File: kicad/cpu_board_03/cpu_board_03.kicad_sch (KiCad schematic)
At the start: 60 parts, among them J1 DIN41612_02x32_AC, J10 PLD_aux, J11 Conn_01x09, J6 Conn_01x02_Socket, J9 Ram1 Enable, SW1 SW_Reset, SW2 SW_PWR, U1 W65C02SxP, U10 74HC245, U11 74HC245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

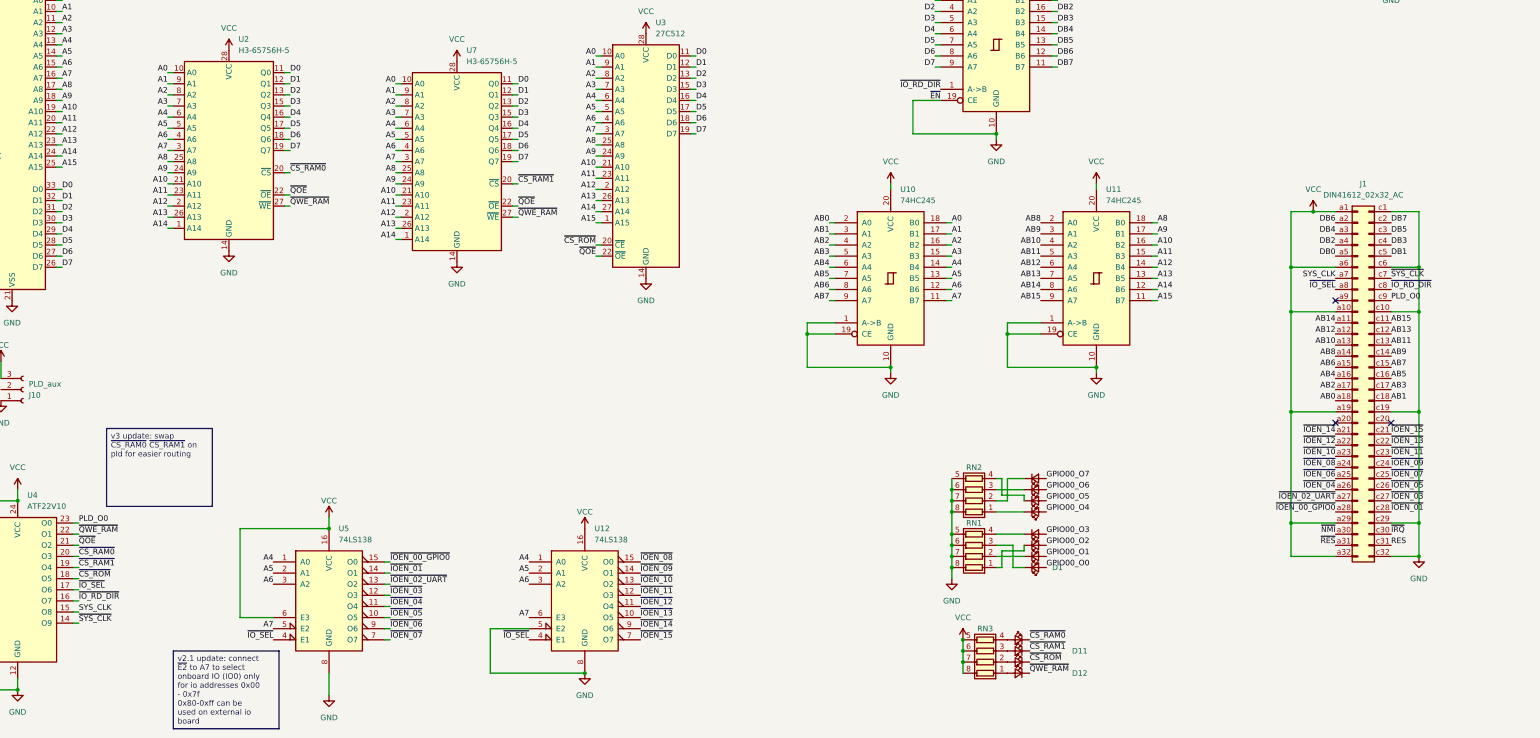
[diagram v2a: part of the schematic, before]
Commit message: update label names
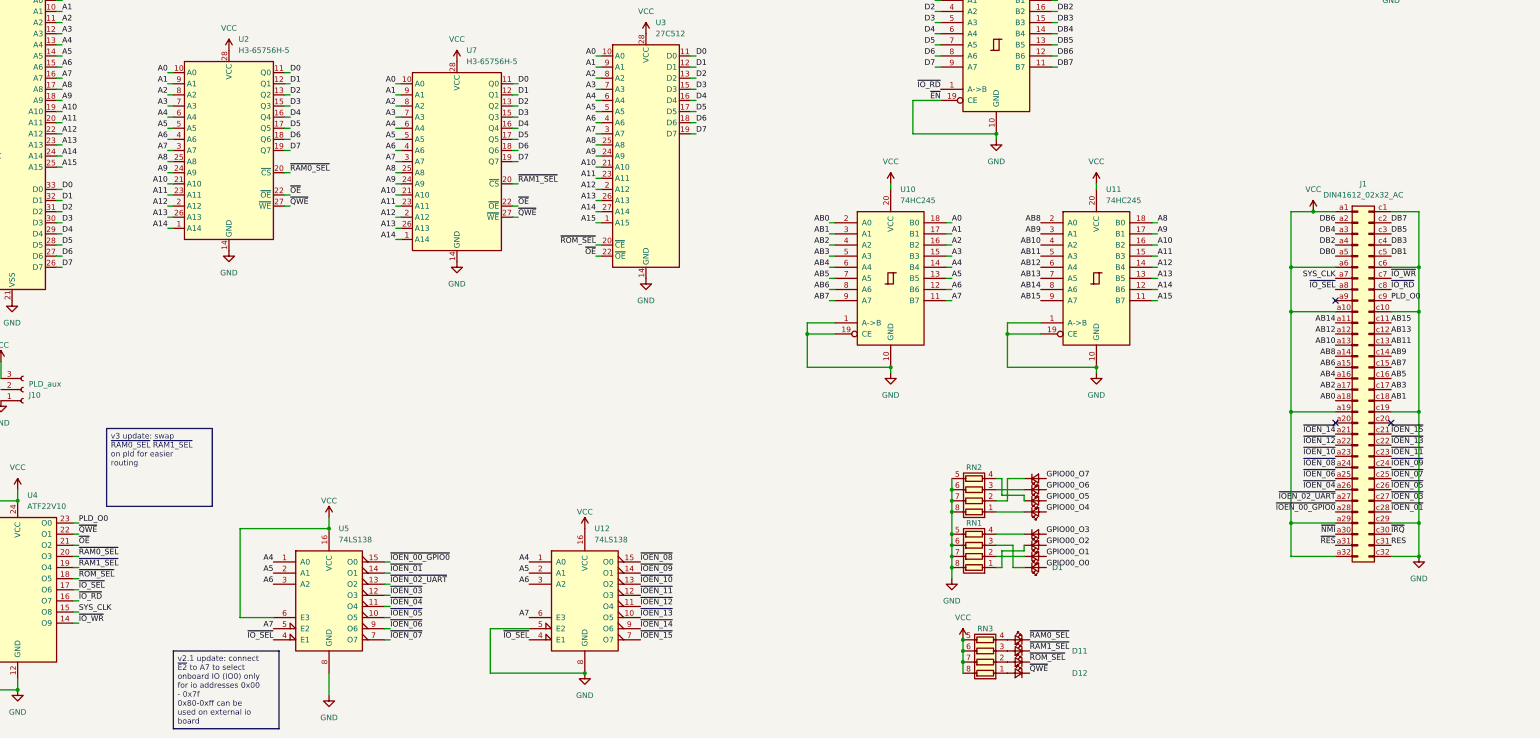
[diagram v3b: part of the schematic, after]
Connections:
- net ~{CS_RAM0} renamed ~{RAM0_SEL}
- net ~{CS_RAM1} renamed ~{RAM1_SEL}
- net ~{CS_ROM} renamed ~{ROM_SEL}
- net ~{IO_RD_DIR} renamed ~{IO_RD}
- net ~{QOE} renamed ~{OE}
- net ~{QWE_RAM} renamed ~{QWE}
- net ~{SYS_CLK} renamed ~{IO_WR}
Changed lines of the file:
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@@
 		)
 	)
-	(text_box "v3 update: swap ~{CS_RAM0} ~{CS_RAM1} on pld for easier routing"
+	(text_box "v3 update: swap ~{RAM0_SEL} ~{RAM1_SEL} on pld for easier routing"
 		(exclude_from_sim no)
 		(at 68.58 214.63 0)
@@
 		)
 	)
-	(label "~{IO_RD_DIR}"
+	(label "~{IO_RD}"
 		(at 361.95 182.88 0)
 		(effects
@@
 		)
 	)
-	(label "~{QOE}"
+	(label "~{OE}"
 		(at 162.56 163.83 0)
 		(effects
@@
 		)
 	)
-	(label "~{IO_RD_DIR}"
+	(label "~{IO_RD}"
 		(at 259.08 137.16 180)
 		(effects
@@
 		)
 	)
-	(label "~{QOE}"
+	(label "~{OE}"
 		(at 62.23 241.3 0)
 		(effects
@@
 		)
 	)
-	(label "~{CS_RAM1}"
+	(label "~{RAM1_SEL}"
 		(at 62.23 246.38 0)
 		(effects
@@
 		)
 	)
-	(label "~{CS_RAM0}"
+	(label "~{RAM0_SEL}"
 		(at 279.4 262.89 0)
 		(effects
@@
 		)
 	)
-	(label "~{QWE_RAM}"
+	(label "~{QWE}"
 		(at 110.49 163.83 0)
 		(effects
@@
 		)
 	)
-	(label "~{QWE_RAM}"
+	(label "~{QWE}"
 		(at 62.23 238.76 0)
 		(effects
@@
 		)
 	)
-	(label "~{CS_RAM0}"
+	(label "~{RAM0_SEL}"
 		(at 62.23 243.84 0)
 		(effects
@@
 		)
 	)
-	(label "~{CS_RAM0}"
+	(label "~{RAM0_SEL}"
 		(at 110.49 156.21 0)
 		(effects
@@
 		)
 	)
-	(label "~{CS_RAM1}"
+	(label "~{RAM1_SEL}"
 		(at 279.4 265.43 0)
 		(effects
@@
 		)
 	)
-	(label "~{QOE}"
+	(label "~{OE}"
 		(at 110.49 161.29 0)
 		(effects
@@
 		)
 	)
-	(label "~{QWE_RAM}"
+	(label "~{QWE}"
 		(at 279.4 270.51 0)
 		(effects
@@
 		)
 	)
-	(label "~{SYS_CLK}"
+	(label "~{IO_WR}"
 		(at 62.23 259.08 0)
 		(effects
@@
 		)
 	)
-	(label "~{IO_RD_DIR}"
+	(label "~{IO_RD}"
 		(at 62.23 254 0)
 		(effects
@@
 		)
 	)
-	(label "~{QWE_RAM}"
+	(label "~{QWE}"
 		(at 162.56 166.37 0)
 		(effects
@@
 		)
 	)
-	(label "~{CS_ROM}"
+	(label "~{ROM_SEL}"
 		(at 62.23 248.92 0)
 		(effects
@@
 		)
 	)
-	(label "~{QOE}"
+	(label "~{OE}"
 		(at 180.34 175.26 180)
 		(effects
@@
 		)
 	)
-	(label "~{CS_ROM}"
+	(label "~{ROM_SEL}"
 		(at 180.34 172.72 180)
 		(effects
@@
 		)
 	)
-	(label "~{SYS_CLK}"
+	(label "~{IO_WR}"
 		(at 361.95 180.34 0)
 		(effects
@@
 		)
 	)
-	(label "~{CS_ROM}"
+	(label "~{ROM_SEL}"
 		(at 279.4 267.97 0)
 		(effects
@@
 		)
 	)
-	(label "~{CS_RAM1}"
+	(label "~{RAM1_SEL}"
 		(at 162.56 158.75 0)
 		(effects

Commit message: update pcb
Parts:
- removed U14: 74AHC1G04, Package_TO_SOT_SMD:SOT-23-5_HandSoldering, symbol 74xGxx:74AHC1G04
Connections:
- net ~{IO_WR}: now also U13.1
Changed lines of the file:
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@@
 	)
 	(no_connect
+		(at 349.25 185.42)
+	)
+	(no_connect
 		(at 349.25 213.36)
 	)
@@
 	)
 	(no_connect
-		(at 349.25 185.42)
-	)
-	(no_connect
 		(at 54.61 52.07)
 	)
@@
 		)
 	)
+	(label "~{IO_WR}"
+		(at 313.69 80.01 180)
+		(effects
+			(font
+				(size 1.27 1.27)
+			)
+			(justify right bottom)
+		)
+	)
 	(label "GPIO00_O4"
 		(at 283.21 233.68 0)
@@
 		)
 	)
-	(label "CLOCK"
-		(at 285.75 80.01 180)
-		(effects
-			(font
-				(size 1.27 1.27)
-			)
-			(justify right bottom)
-		)
-	)
 	(label "A10"
 		(at 308.61 172.72 0)
@@
 	)
 	(symbol
-		(lib_id "74xGxx:74AHC1G04")
-		(at 300.99 80.01 0)
-		(unit 1)
-		(exclude_from_sim no)
-		(in_bom yes)
-		(on_board yes)
-		(dnp no)
-		(fields_autoplaced yes)
-		(property "Reference" "U14"
-			(at 313.69 73.5898 0)
-			(effects
-				(font
-					(size 1.27 1.27)
-				)
-			)
-		)
-		(property "Value" "74AHC1G04"
-			(at 313.69 76.1298 0)
-			(effects
-				(font
-					(size 1.27 1.27)
-				)
-			)
-		)
-		(property "Footprint" "Package_TO_SOT_SMD:SOT-23-5_HandSoldering"
-			(at 300.99 80.01 0)
-			(effects
-				(font
-					(size 1.27 1.27)
-				)
-				(hide yes)
-			)
-		)
-		(property "Datasheet" "http://www.ti.com/lit/sg/scyt129e/scyt129e.pdf"
-			(at 300.99 80.01 0)
-			(effects
-				(font
-					(size 1.27 1.27)
-				)
-				(hide yes)
-			)
-		)
-		(property "Description" "Single NOT Gate, Low-Voltage CMOS"
-			(at 300.99 80.01 0)
-			(effects
-				(font
-					(size 1.27 1.27)
-				)
-				(hide yes)
-			)
-		)
-		(pin "3"
-		)
-		(pin "4"
-		)
-		(pin "5"
-		)
-		(pin "2"
-		)
-		(instances
-			(project ""
-				(path "/a9a73dc6-7f92-4458-9da8-49621d12e480"
-					(reference "U14")
-					(unit 1)
-				)
-			)
-		)
-	)
-	(symbol
 		(lib_id "65xx:W65C02SxP")
 		(at 46.99 147.32 0)
@@
 	)
 	(symbol
+		(lib_id "74xGxx:74AHC1G32")
+		(at 328.93 82.55 0)
+		(unit 1)
+		(exclude_from_sim no)
+		(in_bom yes)
+		(on_board yes)
+		(dnp no)
+		(fields_autoplaced yes)
+		(property "Reference" "U13"
+			(at 341.63 76.1298 0)
+			(effects
+				(font
+					(size 1.27 1.27)
+				)
+			)
+		)
+		(property "Value" "74AHC1G32"
+			(at 341.63 78.6698 0)
+			(effects
+				(font
+					(size 1.27 1.27)
+				)
+			)
+		)
+		(property "Footprint" "Package_TO_SOT_SMD:SOT-23-5_HandSoldering"
+			(at 328.93 82.55 0)
+			(effects
+				(font
+					(size 1.27 1.27)
+				)
+				(hide yes)
+			)
+		)
+		(property "Datasheet" "http://www.ti.com/lit/sg/scyt129e/scyt129e.pdf"
+			(at 328.93 82.55 0)
+			(effects
+				(font
+					(size 1.27 1.27)
+				)
+				(hide yes)
+			)
+		)
+		(property "Description" "Single OR Gate, Low-Voltage CMOS"
+			(at 328.93 82.55 0)
+			(effects
+				(font
+					(size 1.27 1.27)
+				)
+				(hide yes)
+			)
+		)
+		(pin "1"
+		)
+		(pin "3"
+		)
+		(pin "4"
+		)
+		(pin "5"
+		)
+		(pin "2"
+		)
+		(instances
+			(project ""
+				(path "/a9a73dc6-7f92-4458-9da8-49621d12e480"
+					(reference "U13")
+					(unit 1)
+				)
+			)
+		)
+	)
+	(symbol
 		(lib_id "power:GND")
 		(at 46.99 185.42 0)
@@
 	(symbol
 		(lib_id "power:VCC")
-		(at 295.91 69.85 0)
-		(unit 1)
-		(exclude_from_sim no)
-		(in_bom yes)
-		(on_board yes)
-		(dnp no)
-		(fields_autoplaced yes)
-		(property "Reference" "#PWR044"
-			(at 295.91 73.66 0)
-			(effects
-				(font
-					(size 1.27 1.27)
-				)
-				(hide yes)
-			)
-		)
-		(property "Value" "VCC"
-			(at 295.91 64.77 0)
-			(effects
-				(font
-					(size 1.27 1.27)
-				)
-			)
-		)
-		(property "Footprint" ""
-			(at 295.91 69.85 0)
-			(effects
-				(font
-					(size 1.27 1.27)
-				)
-				(hide yes)
-			)
-		)
-		(property "Datasheet" ""
-			(at 295.91 69.85 0)
-			(effects
-				(font
-					(size 1.27 1.27)
-				)
-				(hide yes)
-			)
-		)
-		(property "Description" ""
-			(at 295.91 69.85 0)
-			(effects
-				(font
-					(size 1.27 1.27)
-				)
-			)
-		)
-		(pin "1"
-		)
-		(instances
-			(project "cpu_board_03"
-				(path "/a9a73dc6-7f92-4458-9da8-49621d12e480"
-					(reference "#PWR044")
-					(unit 1)
-				)
-			)
-		)
-	)
-	(symbol
-		(lib_id "power:VCC")
 		(at 48.26 228.6 0)
 		(unit 1)
@@
 	)
 	(symbol
-		(lib_id "74xGxx:74AHC1G32")
-		(at 328.93 82.55 0)
-		(unit 1)
-		(exclude_from_sim no)
-		(in_bom yes)
-		(on_board yes)
-		(dnp no)
-		(fields_autoplaced yes)
-		(property "Reference" "U13"
-			(at 341.63 76.1298 0)
-			(effects
-				(font
-					(size 1.27 1.27)
-				)
-			)
-		)
-		(property "Value" "74AHC1G32"
-			(at 341.63 78.6698 0)
-			(effects
-				(font
-					(size 1.27 1.27)
-				)
-			)
-		)
-		(property "Footprint" "Package_TO_SOT_SMD:SOT-23-5_HandSoldering"
-			(at 328.93 82.55 0)
-			(effects
-				(font
-					(size 1.27 1.27)
-				)
-				(hide yes)
-			)
-		)
-		(property "Datasheet" "http://www.ti.com/lit/sg/scyt129e/scyt129e.pdf"
-			(at 328.93 82.55 0)
-			(effects
-				(font
-					(size 1.27 1.27)
-				)
-				(hide yes)
-			)
-		)
-		(property "Description" "Single OR Gate, Low-Voltage CMOS"
-			(at 328.93 82.55 0)
-			(effects
-				(font
-					(size 1.27 1.27)
-				)
-				(hide yes)
-			)
-		)
-		(pin "1"
-		)
-		(pin "2"
-		)
-		(pin "3"
-		)
-		(pin "5"
-		)
-		(pin "4"
-		)
-		(instances
-			(project ""
-				(path "/a9a73dc6-7f92-4458-9da8-49621d12e480"
-					(reference "U13")
-					(unit 1)
-				)
-			)
-		)
-	)
-	(symbol
 		(lib_id "Device:LED_Small")
 		(at 280.67 243.84 0)
@@
 					(unit 1)
 				)
-			)
-		)
-	)
-	(symbol
-		(lib_id "power:GND")
-		(at 295.91 90.17 0)
-		(unit 1)
-		(exclude_from_sim no)
-		(in_bom yes)
-		(on_board yes)
-		(dnp no)
-		(fields_autoplaced yes)
-		(property "Reference" "#PWR043"
-			(at 295.91 96.52 0)
-			(effects
-				(font
-					(size 1.27 1.27)
-				)
-				(hide yes)
-			)
-		)
-		(property "Value" "GND"
-			(at 295.91 95.25 0)
-			(effects
-				(font
-					(size 1.27 1.27)
-				)
-			)
-		)
-		(property "Footprint" ""
-			(at 295.91 90.17 0)
-			(effects
-				(font
-					(size 1.27 1.27)
-				)
-				(hide yes)
-			)
-		)
-		(property "Datasheet" ""
-			(at 295.91 90.17 0)
-			(effects
-				(font
-					(size 1.27 1.27)
-				)
-				(hide yes)
-			)
-		)
-		(property "Description" ""
-			(at 295.91 90.17 0)
-			(effects
-				(font
-					(size 1.27 1.27)
-				)
-			)
-		)
-		(pin "1"
-		)
-		(instances
-			(project "cpu_board_03"
-				(path "/a9a73dc6-7f92-4458-9da8-49621d12e480"
-					(reference "#PWR043")
-					(unit 1)
-				)
